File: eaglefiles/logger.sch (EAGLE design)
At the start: 39 parts, among them K1 65100516121, Q2 IRLML9301, U1 MCP1640, U3 FT232RLSSOP

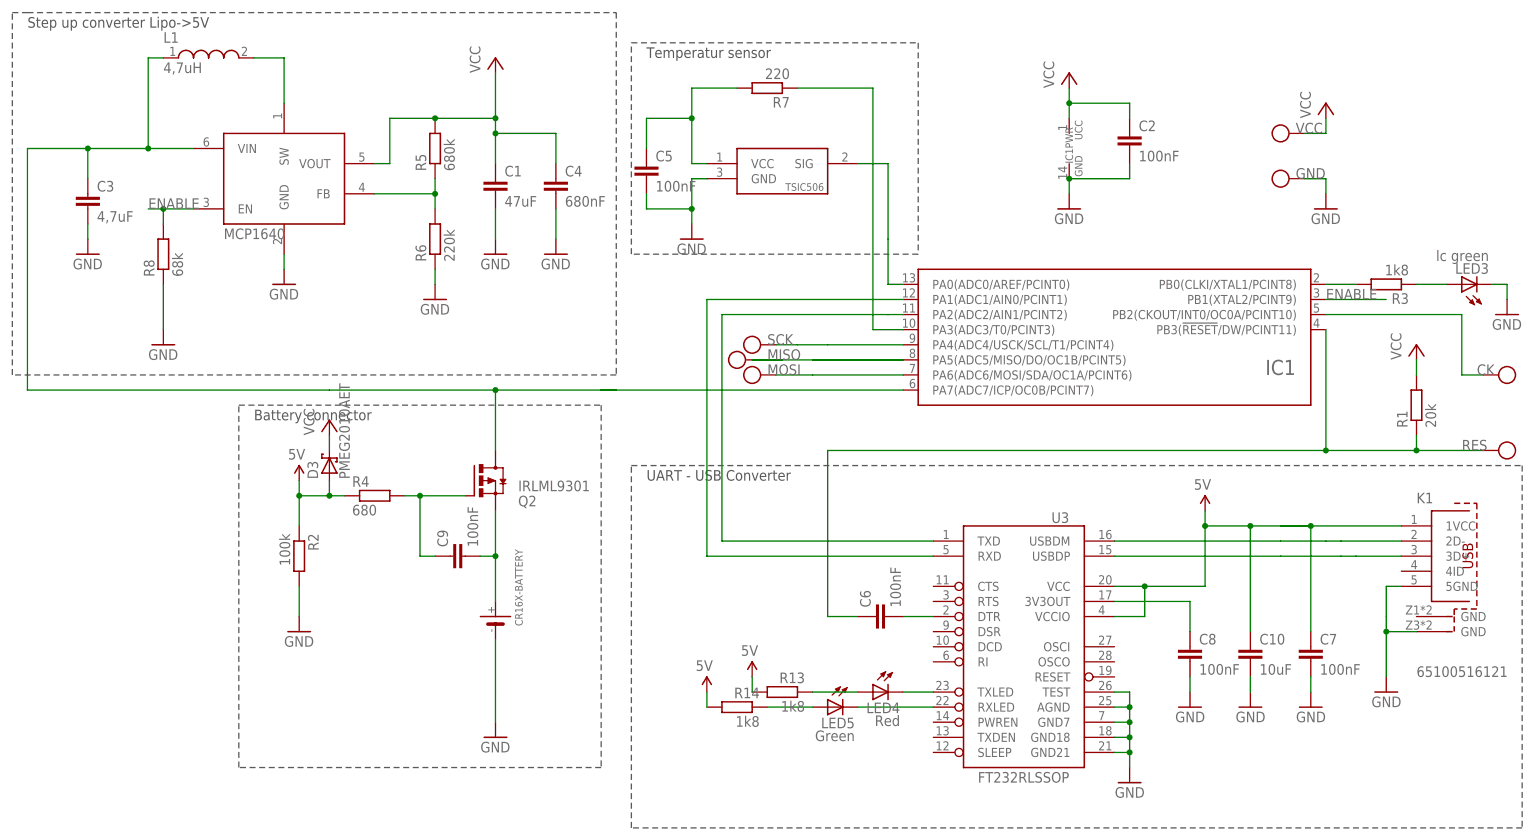
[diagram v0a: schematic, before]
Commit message: Replaced mosfet by diode
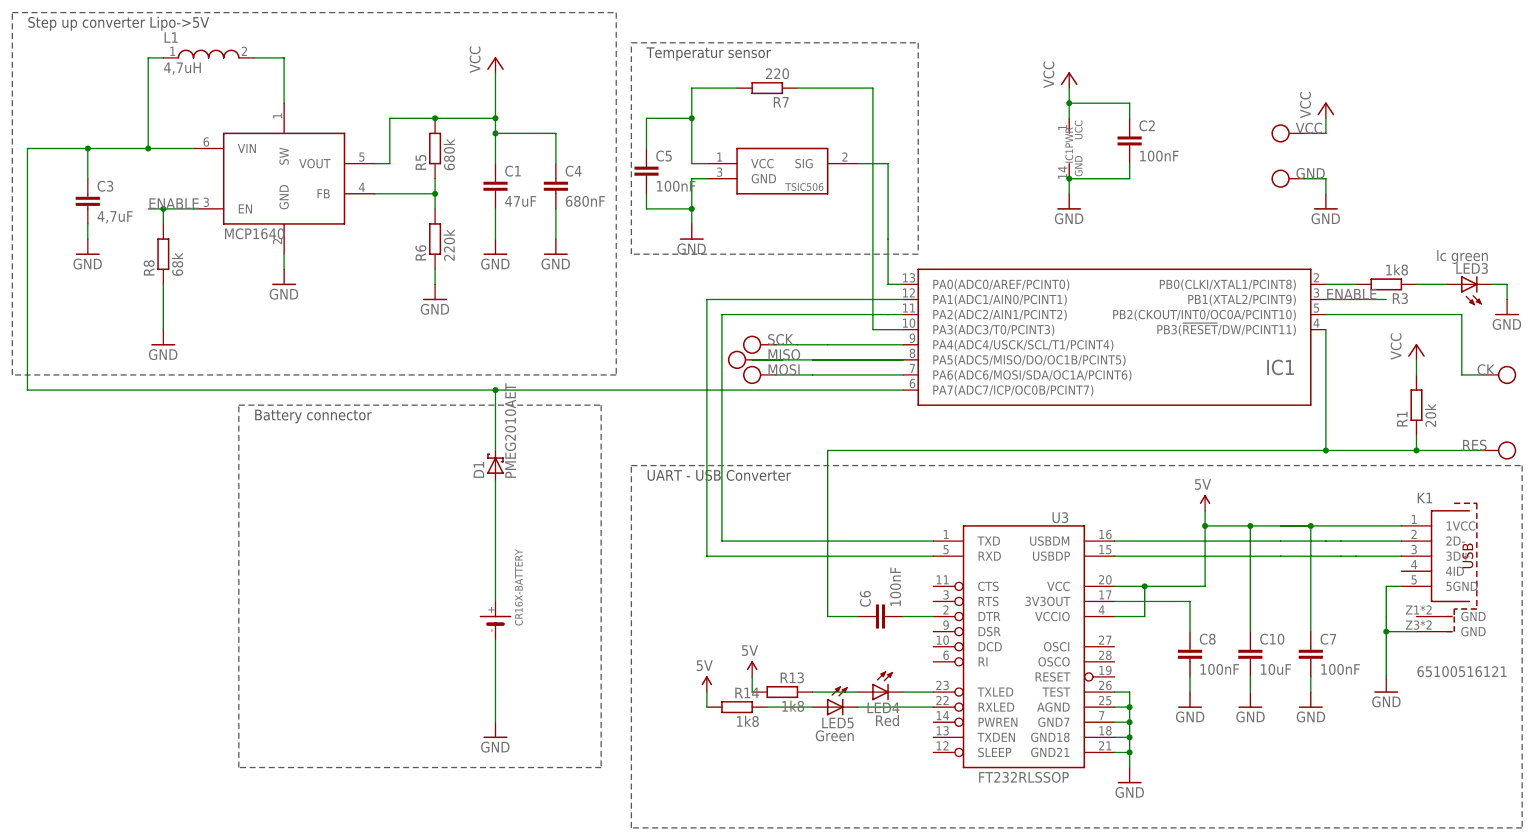
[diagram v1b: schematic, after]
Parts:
- removed C9: 100nF, rcl:C-EUC0603
- removed D3: PMEG2010AET, diode:BAS70
- removed Q2: IRLML9301, 0liver:IRLML9301
- removed R2: 100k, eagle-ltspice:RR1206
- removed R4: 680, eagle-ltspice:RR1206
- added D1: PMEG2010AET, diode:BAS70
- C2, C3: device rcl:C-EUC1206K -> rcl:C-EUC1206
- LED4, LED5: device SparkFun:LED0603 -> led:LEDCHIPLED_0603
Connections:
- removed net BATOFF: C9.1, Q2.G, R4.2
- net GND: no longer R2.2
- net N$6: now also D1.A; no longer C9.2, Q2.S
- net VCC: no longer D3.C
- net VSUPPLY: now also D1.C; no longer Q2.D
- net V_USB: no longer D3.A, R2.1, R4.1
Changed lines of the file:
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@@
 </part>
 <part name="C1" library="resistor" deviceset="C-EU" device="C1206" value="47uF"/>
-<part name="C2" library="rcl" deviceset="C-EU" device="C1206K" value="100nF"/>
+<part name="C2" library="rcl" deviceset="C-EU" device="C1206" value="100nF"/>
 <part name="GND2" library="supply1" deviceset="GND" device=""/>
 <part name="LED3" library="led" deviceset="LED" device="CHIPLED_0603" value="lc green"/>
@@
 <part name="U1" library="karlnet-parts" deviceset="MCP1640" device=""/>
 <part name="GND7" library="supply1" deviceset="GND" device=""/>
-<part name="C3" library="rcl" deviceset="C-EU" device="C1206K" value="4,7uF"/>
+<part name="C3" library="rcl" deviceset="C-EU" device="C1206" value="4,7uF"/>
 <part name="GND8" library="supply1" deviceset="GND" device=""/>
 <part name="R5" library="resistor" deviceset="R-EU_" device="R1206" value="680k"/>
@@
 <part name="R13" library="rcl" deviceset="R-EU_" device="R1206" value="1k8"/>
 <part name="R14" library="rcl" deviceset="R-EU_" device="R1206" value="1k8"/>
-<part name="LED4" library="SparkFun" deviceset="LED" device="0603" value="Red"/>
-<part name="LED5" library="SparkFun" deviceset="LED" device="0603" value="Green"/>
+<part name="LED4" library="led" deviceset="LED" device="CHIPLED_0603" value="Red"/>
+<part name="LED5" library="led" deviceset="LED" device="CHIPLED_0603" value="Green"/>
 <part name="U$5" library="SparkFun" deviceset="5V" device=""/>
 <part name="C7" library="rcl" deviceset="C-EU" device="C1206" value="100nF"/>
@@
 <part name="U$3" library="SparkFun" deviceset="5V" device=""/>
 <part name="U$4" library="SparkFun" deviceset="5V" device=""/>
-<part name="Q2" library="0liver" deviceset="IRLML9301" device=""/>
-<part name="R2" library="eagle-ltspice" deviceset="R" device="R1206" value="100k"/>
-<part name="GND1" library="supply1" deviceset="GND" device=""/>
-<part name="U$6" library="SparkFun" deviceset="5V" device=""/>
 <part name="K1" library="Input-Output_Connectors_rev15d" deviceset="65100516121" device=""/>
 <part name="GND17" library="SparkFun" deviceset="GND" device=""/>
@@
 <part name="U$11" library="0liver" deviceset="PIN" device="1.27"/>
 <part name="U$12" library="0liver" deviceset="PIN" device="1.27"/>
-<part name="C9" library="rcl" deviceset="C-EU" device="C0603" value="100nF"/>
-<part name="R4" library="eagle-ltspice" deviceset="R" device="R1206" value="680"/>
 <part name="C10" library="rcl" deviceset="C-EU" device="C1206" value="10uF"/>
 <part name="C6" library="rcl" deviceset="C-EU" device="C0603" value="100nF"/>
 <part name="R7" library="resistor" deviceset="R-EU_" device="R1206" value="220"/>
-<part name="D3" library="diode" deviceset="BAS70" device="" value="PMEG2010AET"/>
-<part name="P+1" library="supply1" deviceset="VCC" device=""/>
 <part name="R8" library="resistor" deviceset="R-EU_" device="R1206" value="68k"/>
 <part name="GND13" library="supply1" deviceset="GND" device=""/>
 <part name="U$13" library="0liver" deviceset="PIN" device="1.27"/>
+<part name="D1" library="diode" deviceset="BAS70" device="" value="PMEG2010AET"/>
 </parts>
 <sheets>
 <sheet>
 <plain>
-<wire x1="-99.06" y1="71.12" x2="0" y2="71.12" width="0.1524" layer="97" style="shortdash"/>
+<wire x1="-101.6" y1="71.12" x2="0" y2="71.12" width="0.1524" layer="97" style="shortdash"/>
 <wire x1="0" y1="71.12" x2="0" y2="10.16" width="0.1524" layer="97" style="shortdash"/>
 <wire x1="0" y1="10.16" x2="-101.6" y2="10.16" width="0.1524" layer="97" style="shortdash"/>
 <wire x1="-101.6" y1="10.16" x2="-101.6" y2="71.12" width="0.1524" layer="97" style="shortdash"/>
-<wire x1="-101.6" y1="71.12" x2="-99.06" y2="71.12" width="0.1524" layer="97" style="shortdash"/>
 <text x="-99.06" y="68.58" size="1.778" layer="97">Step up converter Lipo-&gt;5V</text>
 <wire x1="2.54" y1="66.04" x2="50.8" y2="66.04" width="0.1524" layer="97" style="shortdash"/>
@@
 <instance part="U$3" gate="G$1" x="22.86" y="-40.64" rot="MR0"/>
 <instance part="U$4" gate="G$1" x="15.24" y="-43.18" rot="MR0"/>
-<instance part="Q2" gate="G$1" x="-22.86" y="-7.62" rot="MR180"/>
-<instance part="R2" gate="G$1" x="-53.34" y="-20.32" rot="R270"/>
-<instance part="GND1" gate="1" x="-53.34" y="-33.02"/>
-<instance part="U$6" gate="G$1" x="-53.34" y="-7.62" rot="MR0"/>
 <instance part="K1" gate="G$1" x="139.7" y="-20.32"/>
 <instance part="GND17" gate="1" x="129.54" y="-43.18" rot="MR0"/>
@@
 <instance part="U$11" gate="G$1" x="22.86" y="10.16" rot="R90"/>
 <instance part="U$12" gate="G$1" x="111.76" y="50.8" rot="R90"/>
-<instance part="C9" gate="G$1" x="-27.94" y="-20.32" rot="R90"/>
-<instance part="R4" gate="G$1" x="-40.64" y="-10.16"/>
 <instance part="C10" gate="G$1" x="106.68" y="-35.56"/>
 <instance part="C6" gate="G$1" x="43.18" y="-30.48" rot="R90"/>
 <instance part="R7" gate="G$1" x="25.4" y="58.42" rot="R180"/>
-<instance part="D3" gate="1" x="-48.26" y="-5.08" rot="R90"/>
-<instance part="P+1" gate="VCC" x="-48.26" y="2.54"/>
 <instance part="R8" gate="G$1" x="-76.2" y="30.48" rot="R90"/>
 <instance part="GND13" gate="1" x="-76.2" y="15.24"/>
 <instance part="U$13" gate="G$1" x="149.86" y="10.16" rot="R270"/>
+<instance part="D1" gate="1" x="-20.32" y="-5.08" rot="R90"/>
 </instances>
 <busses>
@@
 </segment>
 <segment>
-<pinref part="R2" gate="G$1" pin="2"/>
-<pinref part="GND1" gate="1" pin="GND"/>
-<wire x1="-53.34" y1="-25.4" x2="-53.34" y2="-30.48" width="0.1524" layer="91"/>
-</segment>
-<segment>
 <pinref part="K1" gate="G$1" pin="5GND"/>
 <wire x1="132.08" y1="-25.4" x2="129.54" y2="-25.4" width="0.1524" layer="91"/>
@@
 <net name="VSUPPLY" class="0">
 <segment>
-<wire x1="0" y1="7.62" x2="-2.54" y2="7.62" width="0.1524" layer="91"/>
-<wire x1="-20.32" y1="-2.54" x2="-20.32" y2="7.62" width="0.1524" layer="91"/>
-<wire x1="-20.32" y1="7.62" x2="-2.54" y2="7.62" width="0.1524" layer="91"/>
-<wire x1="-2.54" y1="7.62" x2="0" y2="7.62" width="0.1524" layer="91"/>
-<wire x1="-2.54" y1="7.62" x2="0" y2="7.62" width="0.1524" layer="91"/>
 <junction x="-20.32" y="7.62"/>
 <pinref part="U1" gate="G$1" pin="VIN"/>
-<wire x1="-71.12" y1="48.26" x2="-73.66" y2="48.26" width="0.1524" layer="91"/>
-<wire x1="-73.66" y1="48.26" x2="-78.74" y2="48.26" width="0.1524" layer="91"/>
-<wire x1="-78.74" y1="48.26" x2="-81.28" y2="48.26" width="0.1524" layer="91"/>
-<wire x1="-81.28" y1="48.26" x2="-88.9" y2="48.26" width="0.1524" layer="91"/>
-<wire x1="-88.9" y1="48.26" x2="-93.98" y2="48.26" width="0.1524" layer="91"/>
+<wire x1="-71.12" y1="48.26" x2="-78.74" y2="48.26" width="0.1524" layer="91"/>
+<wire x1="-78.74" y1="48.26" x2="-88.9" y2="48.26" width="0.1524" layer="91"/>
 <wire x1="-76.2" y1="63.5" x2="-78.74" y2="63.5" width="0.1524" layer="91"/>
 <wire x1="-78.74" y1="63.5" x2="-78.74" y2="48.26" width="0.1524" layer="91"/>
@@
 <wire x1="-88.9" y1="48.26" x2="-88.9" y2="43.18" width="0.1524" layer="91"/>
 <junction x="-88.9" y="48.26"/>
-<wire x1="-99.06" y1="48.26" x2="-93.98" y2="48.26" width="0.1524" layer="91"/>
+<wire x1="-99.06" y1="48.26" x2="-88.9" y2="48.26" width="0.1524" layer="91"/>
 <pinref part="L1" gate="G$1" pin="1"/>
 <pinref part="IC1" gate="IC" pin="PA7(ADC7/ICP/OC0B/PCINT7)"/>
-<wire x1="48.26" y1="7.62" x2="0" y2="7.62" width="0.1524" layer="91"/>
+<wire x1="48.26" y1="7.62" x2="-20.32" y2="7.62" width="0.1524" layer="91"/>
 <wire x1="-99.06" y1="48.26" x2="-99.06" y2="7.62" width="0.1524" layer="91"/>
-<wire x1="-99.06" y1="7.62" x2="-48.26" y2="7.62" width="0.1524" layer="91"/>
-<pinref part="Q2" gate="G$1" pin="D"/>
-<wire x1="-48.26" y1="7.62" x2="-20.32" y2="7.62" width="0.1524" layer="91"/>
+<wire x1="-99.06" y1="7.62" x2="-20.32" y2="7.62" width="0.1524" layer="91"/>
+<pinref part="D1" gate="1" pin="C"/>
+<wire x1="-20.32" y1="-2.54" x2="-20.32" y2="7.62" width="0.1524" layer="91"/>
 </segment>
 </net>
@@
 <wire x1="-10.16" y1="50.8" x2="-10.16" y2="45.72" width="0.1524" layer="91"/>
 <junction x="-20.32" y="50.8"/>
-</segment>
-<segment>
-<pinref part="D3" gate="1" pin="C"/>
-<pinref part="P+1" gate="VCC" pin="VCC"/>
-<wire x1="-48.26" y1="-2.54" x2="-48.26" y2="0" width="0.1524" layer="91"/>
 </segment>
 </net>
@@
 <pinref part="U$3" gate="G$1" pin="5V"/>
 </segment>
-<segment>
-<pinref part="R2" gate="G$1" pin="1"/>
-<pinref part="R4" gate="G$1" pin="1"/>
-<wire x1="-45.72" y1="-10.16" x2="-48.26" y2="-10.16" width="0.1524" layer="91"/>
-<wire x1="-48.26" y1="-10.16" x2="-53.34" y2="-10.16" width="0.1524" layer="91"/>
-<wire x1="-53.34" y1="-10.16" x2="-53.34" y2="-15.24" width="0.1524" layer="91"/>
-<junction x="-53.34" y="-10.16"/>
-<wire x1="-53.34" y1="-10.16" x2="-53.34" y2="-7.62" width="0.1524" layer="91"/>
-<pinref part="U$6" gate="G$1" pin="5V"/>
-<pinref part="D3" gate="1" pin="A"/>
-<wire x1="-48.26" y1="-10.16" x2="-48.26" y2="-7.62" width="0.1524" layer="91"/>
-<junction x="-48.26" y="-10.16"/>
-</segment>
 </net>
 <net name="N$3" class="0">
@@
 <segment>
 <pinref part="U$1" gate="G$1" pin="P$1"/>
-<wire x1="-20.32" y1="-27.8892" x2="-20.32" y2="-20.32" width="0.1524" layer="91"/>
-<pinref part="C9" gate="G$1" pin="2"/>
-<wire x1="-20.32" y1="-20.32" x2="-22.86" y2="-20.32" width="0.1524" layer="91"/>
-<pinref part="Q2" gate="G$1" pin="S"/>
-<wire x1="-20.32" y1="-12.7" x2="-20.32" y2="-20.32" width="0.1524" layer="91"/>
-<junction x="-20.32" y="-20.32"/>
+<pinref part="D1" gate="1" pin="A"/>
+<wire x1="-20.32" y1="-27.8892" x2="-20.32" y2="-7.62" width="0.1524" layer="91"/>
 </segment>
 </net>
@@
 </segment>
 </net>
-<net name="BATOFF" class="0">
-<segment>
-<wire x1="-25.4" y1="-10.16" x2="-33.02" y2="-10.16" width="0.1524" layer="91"/>
-<pinref part="Q2" gate="G$1" pin="G"/>
-<pinref part="C9" gate="G$1" pin="1"/>
-<wire x1="-30.48" y1="-20.32" x2="-33.02" y2="-20.32" width="0.1524" layer="91"/>
-<wire x1="-33.02" y1="-20.32" x2="-33.02" y2="-10.16" width="0.1524" layer="91"/>
-<pinref part="R4" gate="G$1" pin="2"/>
-<wire x1="-33.02" y1="-10.16" x2="-35.56" y2="-10.16" width="0.1524" layer="91"/>
-<junction x="-33.02" y="-10.16"/>
-</segment>
-</net>

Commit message: Replaced mosfet by diode
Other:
- note removed: "Battery connector"
- moved on the sheet: D1
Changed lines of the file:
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@@
 <part name="LED4" library="led" deviceset="LED" device="CHIPLED_0603" value="Red"/>
 <part name="LED5" library="led" deviceset="LED" device="CHIPLED_0603" value="Green"/>
-<part name="U$5" library="SparkFun" deviceset="5V" device=""/>
 <part name="C7" library="rcl" deviceset="C-EU" device="C1206" value="100nF"/>
 <part name="GND16" library="SparkFun" deviceset="GND" device=""/>
@@
 <plain>
 <wire x1="-101.6" y1="71.12" x2="0" y2="71.12" width="0.1524" layer="97" style="shortdash"/>
-<wire x1="0" y1="71.12" x2="0" y2="10.16" width="0.1524" layer="97" style="shortdash"/>
-<wire x1="0" y1="10.16" x2="-101.6" y2="10.16" width="0.1524" layer="97" style="shortdash"/>
-<wire x1="-101.6" y1="10.16" x2="-101.6" y2="71.12" width="0.1524" layer="97" style="shortdash"/>
+<wire x1="0" y1="71.12" x2="0" y2="-22.86" width="0.1524" layer="97" style="shortdash"/>
+<wire x1="0" y1="-22.86" x2="-101.6" y2="-22.86" width="0.1524" layer="97" style="shortdash"/>
+<wire x1="-101.6" y1="-22.86" x2="-101.6" y2="71.12" width="0.1524" layer="97" style="shortdash"/>
 <text x="-99.06" y="68.58" size="1.778" layer="97">Step up converter Lipo-&gt;5V</text>
 <wire x1="2.54" y1="66.04" x2="50.8" y2="66.04" width="0.1524" layer="97" style="shortdash"/>
@@
 <wire x1="2.54" y1="30.48" x2="2.54" y2="66.04" width="0.1524" layer="97" style="shortdash"/>
 <text x="5.08" y="63.5" size="1.778" layer="97">Temperatur sensor</text>
-<wire x1="-63.5" y1="5.08" x2="-2.54" y2="5.08" width="0.1524" layer="97" style="shortdash"/>
-<wire x1="-2.54" y1="5.08" x2="-2.54" y2="-55.88" width="0.1524" layer="97" style="shortdash"/>
-<wire x1="-2.54" y1="-55.88" x2="-63.5" y2="-55.88" width="0.1524" layer="97" style="shortdash"/>
-<wire x1="-63.5" y1="-55.88" x2="-63.5" y2="5.08" width="0.1524" layer="97" style="shortdash"/>
-<text x="-60.96" y="2.54" size="1.778" layer="97">Battery connector</text>
 <wire x1="2.54" y1="-5.08" x2="152.4" y2="-5.08" width="0.1524" layer="97" style="shortdash"/>
 <wire x1="152.4" y1="-5.08" x2="152.4" y2="-66.04" width="0.1524" layer="97" style="shortdash"/>
@@
 </plain>
 <instances>
-<instance part="U$1" gate="G$1" x="-20.32" y="-30.48" rot="R90"/>
+<instance part="U$1" gate="G$1" x="-20.32" y="-7.62" rot="R90"/>
 <instance part="IC1" gate="IC" x="83.82" y="15.24" smashed="yes">
 <attribute name="UCC" x="83.82" y="15.24" size="1.778" layer="96" display="off"/>
@@
 <instance part="C1" gate="G$1" x="-20.32" y="43.18"/>
 <instance part="C2" gate="G$1" x="86.36" y="50.8"/>
-<instance part="GND2" gate="1" x="-20.32" y="-50.8"/>
+<instance part="GND2" gate="1" x="-20.32" y="-15.24"/>
 <instance part="LED3" gate="G$1" x="142.24" y="25.4" rot="R90"/>
 <instance part="R3" gate="G$1" x="129.54" y="25.4" rot="R180"/>
@@
 <instance part="LED4" gate="G$1" x="43.18" y="-43.18" rot="MR270"/>
 <instance part="LED5" gate="G$1" x="35.56" y="-45.72" rot="MR270"/>
-<instance part="U$5" gate="G$1" x="99.06" y="-12.7" rot="MR0"/>
 <instance part="C7" gate="G$1" x="116.84" y="-35.56"/>
 <instance part="GND16" gate="1" x="96.52" y="-45.72" rot="MR0"/>
@@
 <instance part="GND13" gate="1" x="-76.2" y="15.24"/>
 <instance part="U$13" gate="G$1" x="149.86" y="10.16" rot="R270"/>
-<instance part="D1" gate="1" x="-20.32" y="-5.08" rot="R90"/>
+<instance part="D1" gate="1" x="-20.32" y="0" rot="R90"/>
 </instances>
 <busses>
@@
 <net name="GND" class="0">
 <segment>
-<wire x1="-20.32" y1="-43.18" x2="-20.32" y2="-48.26" width="0.1524" layer="91"/>
 <pinref part="GND2" gate="1" pin="GND"/>
-<wire x1="-20.32" y1="-43.18" x2="-20.32" y2="-34.417" width="0.1524" layer="91"/>
+<wire x1="-20.32" y1="-12.7" x2="-20.32" y2="-11.557" width="0.1524" layer="91"/>
 <pinref part="U$1" gate="G$1" pin="P$2"/>
 </segment>
@@
 <wire x1="-99.06" y1="7.62" x2="-20.32" y2="7.62" width="0.1524" layer="91"/>
 <pinref part="D1" gate="1" pin="C"/>
-<wire x1="-20.32" y1="-2.54" x2="-20.32" y2="7.62" width="0.1524" layer="91"/>
+<wire x1="-20.32" y1="2.54" x2="-20.32" y2="7.62" width="0.1524" layer="91"/>
 </segment>
 </net>
@@
 <wire x1="116.84" y1="-33.02" x2="116.84" y2="-15.24" width="0.1524" layer="91"/>
 <wire x1="111.76" y1="-15.24" x2="116.84" y2="-15.24" width="0.1524" layer="91"/>
-<wire x1="99.06" y1="-12.7" x2="99.06" y2="-15.24" width="0.1524" layer="91"/>
 <junction x="106.68" y="-15.24"/>
 <junction x="116.84" y="-15.24"/>
-<junction x="99.06" y="-15.24"/>
 <pinref part="U3" gate="G$1" pin="VCC"/>
-<pinref part="U$5" gate="G$1" pin="5V"/>
 <pinref part="C7" gate="G$1" pin="1"/>
 <pinref part="U3" gate="G$1" pin="VCCIO"/>
@@
 <junction x="88.9" y="-25.4"/>
 <pinref part="K1" gate="G$1" pin="1VCC"/>
-<wire x1="111.76" y1="-15.24" x2="132.08" y2="-15.24" width="0.1524" layer="91"/>
+<wire x1="116.84" y1="-15.24" x2="132.08" y2="-15.24" width="0.1524" layer="91"/>
 <pinref part="C10" gate="G$1" pin="1"/>
 </segment>
@@
 <pinref part="U$1" gate="G$1" pin="P$1"/>
 <pinref part="D1" gate="1" pin="A"/>
-<wire x1="-20.32" y1="-27.8892" x2="-20.32" y2="-7.62" width="0.1524" layer="91"/>
-</segment>
-</net>
+<wire x1="-20.32" y1="-5.0292" x2="-20.32" y2="-2.54" width="0.1524" layer="91"/>
+</segment>
+</net>
